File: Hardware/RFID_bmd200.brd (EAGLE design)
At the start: 74.9 x 34 mm, 48 parts, among them IC1 EM4095, IC2 STM32F334K

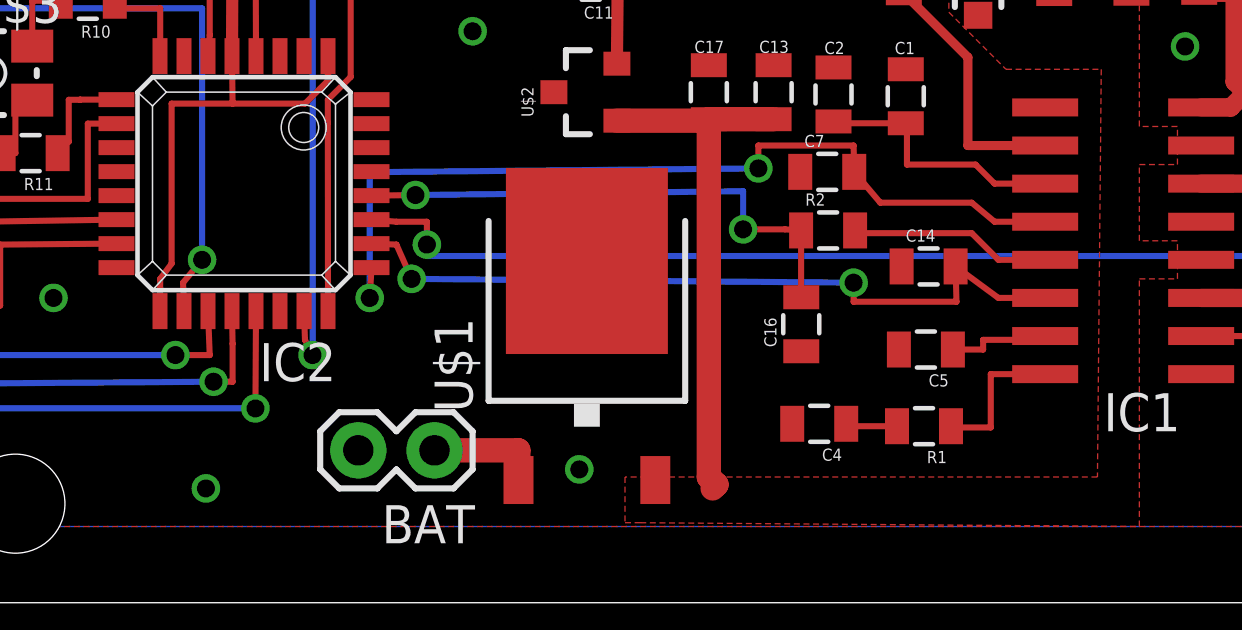
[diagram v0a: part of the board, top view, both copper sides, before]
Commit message: fixed some missing grounds and changed to the RTS pin on the STM32F334
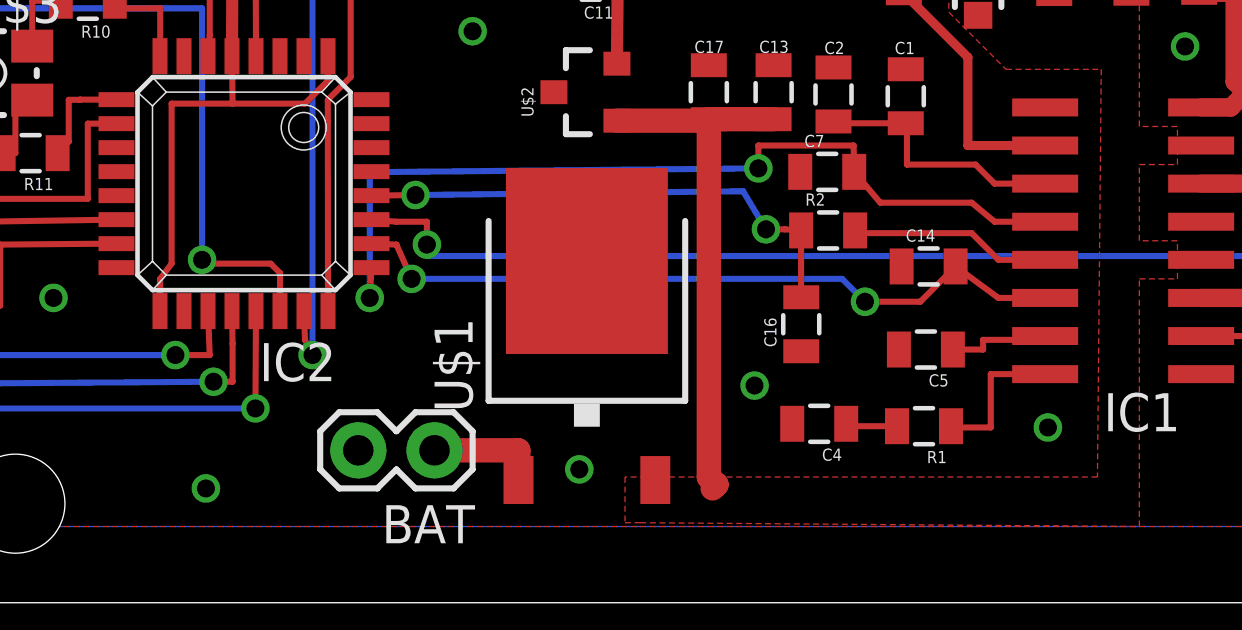
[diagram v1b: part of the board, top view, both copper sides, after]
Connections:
- net N$4: now also IC2.22; no longer IC2.18
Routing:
- net N$4: track 24.5 -> 26.6 mm
- net SHD: track 25.4 -> 24.3 mm
- net DMOD_OUT: track 17.8 -> 17.3 mm
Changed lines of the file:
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@@
 </elements>
 <signals>
-<signal name="GND" airwireshidden="yes">
+<signal name="GND">
 <contactref element="U$1" pad="4"/>
 <contactref element="C17" pad="2"/>
@@
 <via x="66.04" y="19.05" extent="1-16" drill="0.6"/>
 <via x="61.849" y="17.272" extent="1-16" drill="0.6"/>
-<wire x1="49.021" y1="13.092" x2="50.13" y2="16.572" width="0" layer="19" extent="1-1"/>
-<wire x1="52.4" y1="9.94" x2="49.021" y2="13.092" width="0" layer="19" extent="1-1"/>
-<wire x1="52.31" y1="7.17" x2="52.4" y2="9.94" width="0" layer="19" extent="1-1"/>
+<via x="47.498" y="5.969" extent="1-16" drill="0.6"/>
+<via x="57.277" y="4.572" extent="1-16" drill="0.6"/>
 </signal>
 <signal name="5V">
@@
 <wire x1="35.56" y1="10.668" x2="36.068" y2="9.525" width="0.2032" layer="1"/>
 <via x="36.068" y="9.525" extent="1-16" drill="0.6"/>
-<wire x1="36.068" y1="9.525" x2="50.8" y2="9.398" width="0.2032" layer="16"/>
-<via x="50.8" y="9.398" extent="1-16" drill="0.6"/>
-<wire x1="50.8" y1="9.398" x2="50.8" y2="8.763" width="0.2032" layer="1"/>
-<wire x1="50.8" y1="8.763" x2="54.229" y2="8.763" width="0.2032" layer="1"/>
-<wire x1="54.229" y1="8.763" x2="54.2" y2="9.94" width="0.2032" layer="1"/>
+<wire x1="36.068" y1="9.525" x2="50.419" y2="9.525" width="0.2032" layer="16"/>
+<wire x1="50.419" y1="9.525" x2="51.181" y2="8.763" width="0.2032" layer="16"/>
+<via x="51.181" y="8.763" extent="1-16" drill="0.6"/>
+<wire x1="51.181" y1="8.763" x2="53.023" y2="8.763" width="0.2032" layer="1"/>
+<wire x1="53.023" y1="8.763" x2="54.2" y2="9.94" width="0.2032" layer="1"/>
 </signal>
 <signal name="MOD">
@@
 <via x="36.195" y="12.319" extent="1-16" drill="0.6"/>
 <wire x1="36.195" y1="12.319" x2="47.117" y2="12.446" width="0.2032" layer="16"/>
-<wire x1="47.117" y1="12.446" x2="47.117" y2="11.176" width="0.2032" layer="16"/>
-<via x="47.117" y="11.176" extent="1-16" drill="0.6"/>
-<wire x1="47.117" y1="11.176" x2="48.514" y2="11.176" width="0.2032" layer="1"/>
+<wire x1="47.117" y1="12.446" x2="47.879" y2="11.176" width="0.2032" layer="16"/>
+<via x="47.879" y="11.176" extent="1-16" drill="0.6"/>
+<wire x1="47.879" y1="11.176" x2="48.514" y2="11.176" width="0.2032" layer="1"/>
 <wire x1="48.514" y1="11.176" x2="49.05" y2="11.14" width="0.2032" layer="1"/>
 </signal>
@@
 </signal>
 <signal name="N$4">
-<contactref element="IC2" pad="18"/>
 <contactref element="U1" pad="20"/>
-<wire x1="28.48" y1="8.45" x2="28.448" y2="9.398" width="0.2032" layer="1"/>
-<wire x1="28.448" y1="9.398" x2="29.083" y2="10.16" width="0.2032" layer="1"/>
 <via x="29.083" y="10.16" extent="1-16" drill="0.6"/>
 <wire x1="29.083" y1="10.16" x2="29.083" y2="18.542" width="0.2032" layer="16"/>
@@
 <via x="16.383" y="18.542" extent="1-16" drill="0.6"/>
 <wire x1="16.383" y1="18.542" x2="14.89" y2="18.41" width="0.2032" layer="1"/>
+<contactref element="IC2" pad="22"/>
+<wire x1="31.68" y1="8.45" x2="31.68" y2="9.722" width="0.2032" layer="1"/>
+<wire x1="31.68" y1="9.722" x2="31.369" y2="10.033" width="0.2032" layer="1"/>
+<wire x1="31.369" y1="10.033" x2="29.21" y2="10.033" width="0.2032" layer="1"/>
+<wire x1="29.21" y1="10.033" x2="29.083" y2="10.16" width="0.2032" layer="1"/>
 </signal>
 <signal name="N$8">
